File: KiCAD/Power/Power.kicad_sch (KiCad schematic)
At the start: 2 parts, among them U1 LM317L_SOT-89, U2 LM337_SOT223

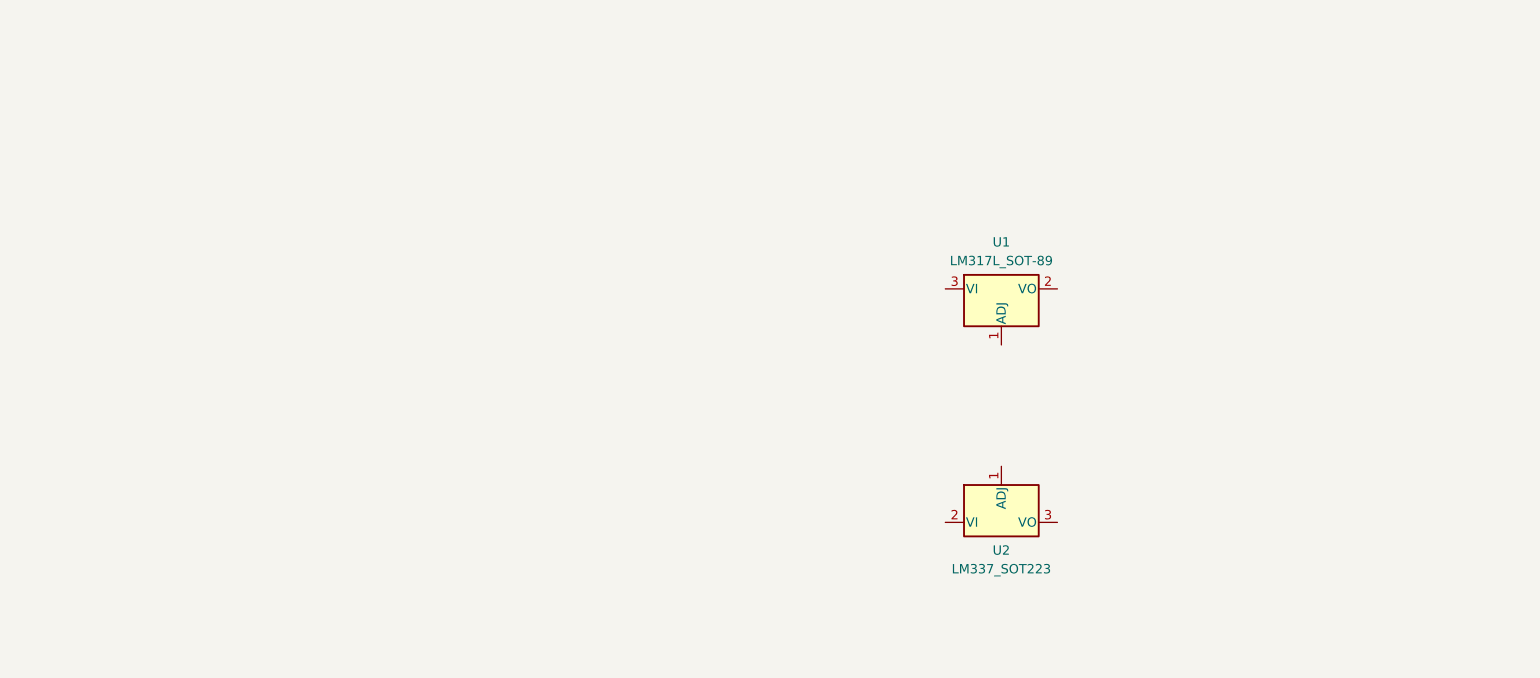
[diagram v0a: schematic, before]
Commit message: Power Schematic and Libraries
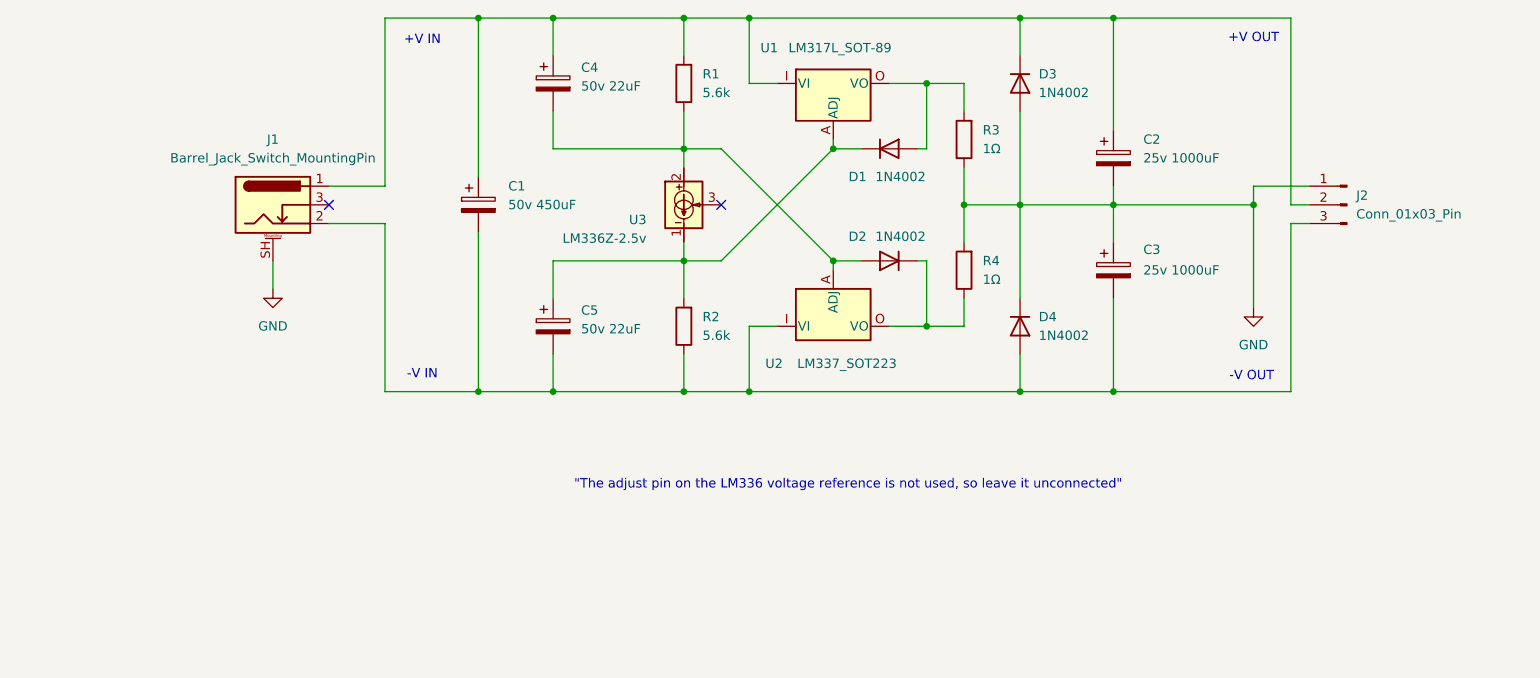
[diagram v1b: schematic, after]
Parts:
- added C1: 50v 450uF, Capacitor_THT:CP_Radial_D10.0mm_P5.00mm, symbol Device:C_Polarized
- added C2, C3: 25v 1000uF, Capacitor_THT:CP_Radial_D10.0mm_P5.00mm, symbol Device:C_Polarized
- added C4, C5: 50v 22uF, Capacitor_THT:CP_Radial_D5.0mm_P2.50mm, symbol Device:C_Polarized
- added D1, D2, D3, D4: 1N4002, Diode_THT:D_A-405_P7.62mm_Horizontal, symbol Device:D
- added J1: Barrel_Jack_Switch_MountingPin, HackSynth:BarrelJack_DC044A, symbol HackSynth:Barrel_Jack_Switch_MountingPin
- added J2: Conn_01x03_Pin, HackSynth:JST_PH_S3B-PH-K_1x03_P2.00mm_Horizontal, symbol Connector:Conn_01x03_Pin
- added R1, R2: 5.6k, Resistor_THT:R_Axial_DIN0207_L6.3mm_D2.5mm_P7.62mm_Horizontal, symbol HackSynth:R
- added R3, R4: 1Ω, Resistor_THT:R_Axial_DIN0207_L6.3mm_D2.5mm_P7.62mm_Horizontal, symbol HackSynth:R
- added U3: LM336Z-2.5v, HackSynth:TO-92_Inline - Handsolder, symbol HackSynth:LM336Z
- U1: footprint Package_TO_SOT_SMD:SOT-89-3 -> HackSynth:LM317 - TO-220-3_Vertical
- U2: footprint Package_TO_SOT_SMD:SOT-223-3_TabPin2 -> HackSynth:LM337 - TO-220-3_Vertical
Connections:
- new net: D1.2 (A), R3.2, U1.O (VO)
- new net: C1.2, C3.2, C5.2, D4.2 (A), J1.2, J2.3 (Pin_3), R2.1, U2.I (VI)
- new net: C4.2, D2.2 (A), R1.1, U2.A (ADJ), U3.2
- new net: C1.1, C2.1, C4.1, D3.1 (K), J1.1, J2.2 (Pin_2), R1.2, U1.I (VI)
- new net: D2.1 (K), R4.1, U2.O (VO)
- new net: C5.1, D1.1 (K), R2.2, U1.A (ADJ), U3.1
- new net GND: C2.2, C3.1, D3.2 (A), D4.1 (K), J1.SH (MountPin), J2.1 (Pin_1), R3.1, R4.2
- no-connect marks 0 -> 2
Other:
- note added: ""The adjust pin on the LM336 voltage reference is not used, so leave it unconnected""
- note added: "+V IN"
- note added: "+V OUT"
- note added: "-V IN"
- note added: "-V OUT"
- moved on the sheet: U1, U2

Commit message: MidMount Capacitors
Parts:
- removed U1: LM317L_SOT-89, HackSynth:LM317 - TO-220-3_Vertical, symbol Regulator_Linear:LM317L_SOT-89
- removed U2: LM337_SOT223, HackSynth:LM337 - TO-220-3_Vertical, symbol Regulator_Linear:LM337_SOT223
- added U1: LM317 TO-220, HackSynth:LM317 - TO-220-3_Horizontal_TabDown, symbol HackSynth:LM317 TO-220
- added U2: LM337 TO-220, HackSynth:LM337 - TO-220-3_Horizontal_TabDown, symbol HackSynth:LM337 TO-220
- C1, C2, C3: footprint Capacitor_THT:CP_Radial_D10.0mm_P5.00mm -> HackSynth:CP_Radial_D10.0mm_P5.00mm_MidMount
- U3: footprint HackSynth:TO-92_Inline - Handsolder -> Package_TO_SOT_THT:TO-92_Inline
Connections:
- net at D1.2 (A), R3.2: now also U1.O (VO)
- net at C1.2, C3.2, C5.2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: now also U2.I (VI)
- net at C4.2, D2.2 (A), R1.1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: now also U2.A (ADJ)
- net at C1.1, C2.1, C4.1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: now also U1.I (VI)
- net at D2.1 (K), R4.1: now also U2.O (VO)
- net at C5.1, D1.1 (K), R2.2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: now also U1.A (ADJ)
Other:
- note removed: ""The adjust pin on the LM336 voltage reference is not used, so leave it unconnected""
- moved on the sheet: C1, C2, C3, C4, C5, D1, D2, D3, D4, J1, J2, R1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

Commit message: Power PCB
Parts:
- U3: footprint Package_TO_SOT_THT:TO-92_Inline -> HackSynth:TO-92_Inline - Handsolder
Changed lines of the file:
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@@
 			)
 		)
-		(property "Footprint" "Package_TO_SOT_THT:TO-92_Inline"
+		(property "Footprint" "HackSynth:TO-92_Inline - Handsolder"
 			(at 120.015 89.535 0)
 			(effects

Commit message: Power PCB
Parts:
- C4, C5: footprint Capacitor_THT:CP_Radial_D5.0mm_P2.50mm -> HackSynth:CP_Radial_D5.2mm_P2.50mm_LayDown
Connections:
- net VSS: now reaches C1.2, C3.2, C5.2, D4.2 (A), J1.2, J2.3 (Pin_3), R2.1, U2.I (VI)
- net VDD: now reaches C1.1, C2.1, C4.1, D3.1 (K), J1.1, J2.2 (Pin_2), R1.2, U1.I (VI)
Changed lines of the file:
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@@
+	)
+	(junction
+		(at 210.82 59.69)
+		(diameter 0)
+		(color 0 0 0 0)
 	)
 	(junction
@@
 	)
 	(junction
+		(at 210.82 110.49)
+		(diameter 0)
+		(color 0 0 0 0)
+	)
+	(junction
 		(at 157.48 101.6)
 		(diameter 0)
@@
 	(wire
 		(pts
+			(xy 210.82 113.03) (xy 210.82 110.49)
+		)
+		(stroke
+			(width 0)
+			(type default)
+		)
+	)
+	(wire
+		(pts
 			(xy 173.99 110.49) (xy 186.69 110.49)
 		)
@@
 		(pts
 			(xy 119.38 77.47) (xy 119.38 80.01)
+		)
+		(stroke
+			(width 0)
+			(type default)
+		)
+	)
+	(wire
+		(pts
+			(xy 210.82 57.15) (xy 210.82 59.69)
 		)
 		(stroke
@@
 			)
 		)
-		(property "Footprint" "Capacitor_THT:CP_Radial_D5.0mm_P2.50mm"
+		(property "Footprint" "HackSynth:CP_Radial_D5.2mm_P2.50mm_LayDown"
 			(at 102.5652 72.39 0)
 			(effects
@@
 				(path "/3945dfa0-e411-40a6-854a-cc3b33a69c85"
 					(reference "D2")
+					(unit 1)
+				)
+			)
+		)
+	)
+	(symbol
+		(lib_id "power:VDD")
+		(at 210.82 57.15 0)
+		(unit 1)
+		(exclude_from_sim no)
+		(in_bom yes)
+		(on_board yes)
+		(dnp no)
+		(fields_autoplaced yes)
+		(property "Reference" "#PWR04"
+			(at 210.82 60.96 0)
+			(effects
+				(font
+					(size 1.27 1.27)
+				)
+				(hide yes)
+			)
+		)
+		(property "Value" "VDD"
+			(at 210.82 52.07 0)
+			(effects
+				(font
+					(size 1.27 1.27)
+				)
+			)
+		)
+		(property "Footprint" ""
+			(at 210.82 57.15 0)
+			(effects
+				(font
+					(size 1.27 1.27)
+				)
+				(hide yes)
+			)
+		)
+		(property "Datasheet" ""
+			(at 210.82 57.15 0)
+			(effects
+				(font
+					(size 1.27 1.27)
+				)
+				(hide yes)
+			)
+		)
+		(property "Description" "Power symbol creates a global label with name \"VDD\""
+			(at 210.82 57.15 0)
+			(effects
+				(font
+					(size 1.27 1.27)
+				)
+				(hide yes)
+			)
+		)
+		(pin "1"
+		)
+		(instances
+			(project ""
+				(path "/3945dfa0-e411-40a6-854a-cc3b33a69c85"
+					(reference "#PWR04")
 					(unit 1)
 				)
@@
 			)
 		)
-		(property "Footprint" "Capacitor_THT:CP_Radial_D5.0mm_P2.50mm"
+		(property "Footprint" "HackSynth:CP_Radial_D5.2mm_P2.50mm_LayDown"
 			(at 102.5652 105.41 0)
 			(effects
@@
 					(unit 1)
 				)
+			)
+		)
+	)
+	(symbol
+		(lib_id "power:VSS")
+		(at 210.82 113.03 180)
+		(unit 1)
+		(exclude_from_sim no)
+		(in_bom yes)
+		(on_board yes)
+		(dnp no)
+		(property "Reference" "#PWR03"
+			(at 210.82 109.22 0)
+			(effects
+				(font
+					(size 1.27 1.27)
+				)
+				(hide yes)
+			)
+		)
+		(property "Value" "VSS"
+			(at 210.82 118.11 0)
+			(effects
+				(font
+					(size 1.27 1.27)
+				)
+			)
+		)
+		(property "Footprint" ""
+			(at 210.82 113.03 0)
+			(effects
+				(font
+					(size 1.27 1.27)
+				)
+				(hide yes)
+			)
+		)
+		(property "Datasheet" ""
+			(at 210.82 113.03 0)
+			(effects
+				(font
+					(size 1.27 1.27)
+				)
+				(hide yes)
+			)
+		)
+		(property "Description" "Power symbol creates a global label with name \"VSS\""
+			(at 210.82 113.03 0)
+			(effects
+				(font
+					(size 1.27 1.27)
+				)
+				(hide yes)
+			)
+		)
+		(pin "1"
+		)
+		(instances
+			(project ""
+				(path "/3945dfa0-e411-40a6-854a-cc3b33a69c85"
+					(reference "#PWR03")
+					(unit 1)
+				)

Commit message: Power PCB
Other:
- note added: "3v LED + 4.7k Resistor"
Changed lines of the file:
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@@
 	(generator_version "9.0")
 	(paper "A4")
+	(text "3v LED + 4.7k Resistor"
+		(exclude_from_sim no)
+		(at 90.17 38.1 0)
+		(effects
+			(font
+				(size 1.27 1.27)
+			)
+		)
+	)
 	(text "-V OUT\n"
 		(exclude_from_sim no)

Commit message: Power PCB Gerbers
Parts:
- added D5: LED, HackSynth:LED_D5.0mm, symbol Device:LED
- added R5: 1.1k, Resistor_THT:R_Axial_DIN0207_L6.3mm_D2.5mm_P7.62mm_Horizontal, symbol HackSynth:R
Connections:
- net VDD: now also D5.2 (A)
- net VSS: now also R5.1
- new net: D5.1 (K), R5.2
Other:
- moved on the sheet: J1
